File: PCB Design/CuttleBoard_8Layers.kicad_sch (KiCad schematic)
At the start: 170 parts, among them IC1 W25Q256JVEIQ TR, J1 DX07WH24JA3R1200, SW1 SW_Push, SW2 SW_Push, U1 LMR33630CQRNX, U14 STM32H743VIHx, U15 TPS62824ADMQ, U16 ICM-20602, U19 USBLC6-2P6, U20 ACS722xLCTR-10AB, U3 LMR33630CQRNX, U4 ICM-20602, U7 MPRLS0025PA00001A, Y1 NX2016SA

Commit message: Revert "STM32H743 first version"
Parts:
- removed C14, C16: 4.7µF, Capacitor_SMD:C_0402_1005Metric, symbol Device:C
- removed C19: 100nF, Capacitor_SMD:C_0402_1005Metric, symbol Device:C
- removed SW2: SW_Push, Button_Switch_SMD:SW_Push_1P1T-SH_NO_CK_KMR2xxG, symbol Switch:SW_Push
- removed U14: STM32H743VIHx, Package_BGA:TFBGA-100_8x8mm_Layout10x10_P0.8mm, symbol MCU_ST_STM32H7:STM32H743VIHx
- added C21, C22, C23: 4.7µF, Capacitor_SMD:C_0402_1005Metric, symbol Device:C
- added L3: 2.2µH, Inductor_SMD:L_0603_1608Metric, symbol pspice:INDUCTOR
- added U2: STM32H735VGH6, Package_BGA:TFBGA-100_8x8mm_Layout10x10_P0.8mm, symbol ultimateFC-rescue:STM32H735VGH6-lib_ultimateFC
- R20: value 10k -> 2k2; footprint ultimateFC:R_0201_0603Metric_mod -> Resistor_SMD:R_0402_1005Metric; JLCPCB Part # (none) -> C2076947
- R9: value 2k2 -> 10k; footprint Resistor_SMD:R_0402_1005Metric -> ultimateFC:R_0201_0603Metric_mod; JLCPCB Part # C2076947 -> (none)
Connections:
- net CS_FLASH: now also U2.C3 (PE4)
- net CS_IMU1: now also U2.A9 (PD2)
- net EOC_PRESSURE: now also U2.A1 (PE6)
- net GND: now also R20.2, C21.2, C22.2, C23.2, U2.C1 (VSS), U2.D1 (VSSSMPS), U2.D5 (VSS), U2.E7 (VSS), U2.F5 (VSS), U2.H2 (VSSA); no longer R9.2
- net I2C1_SCL: now also U2.D4 (PB6)
- net I2C1_SDA: now also U2.B5 (PB7)
- net I2C2_SCL: now also U2.K7 (PB10)
- net I2C2_SDA: now also U2.J7 (PB11)
- net I2C3_SCL: now also U2.F10 (PA8)
- net I2C3_SDA: now also U2.F9 (PC9)
- net I2C4_SCL: now also U2.A4 (PB8)
- net I2C4_SDA: now also U2.E3 (PB9)
- net INT_IMU1: now also U2.A8 (PD3)
- net NRST: now also R9.2, U2.F2 (NRST); no longer R20.2
- net OSC_IN: now also C7.1, U2.G1 (PH0-OSC_IN); no longer C9.1
- net OSC_OUT: now also C9.1, U2.G2 (PH1-OSC_OUT); no longer C7.1
- net RES_PRESSURE: now also U2.A2 (PE5)
- net SWDCLK: now also U2.C9 (PA14)
- net SWDIO: now also U2.C10 (PA13)
- net UART3_RX: now also U2.H8 (PD9)
- net UART3_TX: now also U2.J9 (PD8)
- net UART7_RX: now also U2.H5 (PE7)
- net UART7_TX: now also U2.J6 (PE8)
- net USB_D+: now also U2.D9 (PA12)
- net USB_D-: now also U2.D10 (PA11)
- net VSense: now also U2.H4 (PC4)
- net curr_sig: now also U2.J3 (PA6)
- net PA9_USB_VBUS_sense: now reaches R14.2, R15.1, TP81.1
- net PA9_USB_VBUS_sense: now also U2.E9 (PA9)
- net +3.3V renamed +3V3
- net +3V3: now also R9.1, U2.C2 (VBAT), U2.D3 (PDR_ON), U2.D6 (VDD), U2.E1 (VDDSMPS), U2.E5 (VDD), U2.E8 (VDD33USB), U2.F6 (VDD), U2.H1 (VDDA), U2.J1 (VREF+); no longer R20.1
- net BOOT0: no longer names the net of SW1.1
- net BOOT0: now also R20.1, U2.A5 (BOOT0); no longer R9.1
- net INT1_IMU3 renamed INT_IMU31
- net INT2_IMU3 renamed INT_IMU32
- net LED_BL renamed PC8_LED_BL
- net PC8_LED_BL: now also U2.G10 (PC8)
- net LED_WT renamed PC7_LED_WT
- net PC7_LED_WT: now also U2.G9 (PC7)
- net SPI3_MISO renamed MISO_GYRO
- net MISO_GYRO: now also U2.B9 (PC11)
- net SPI3_MOSI renamed MOSI_GYRO
- net MOSI_GYRO: now also U2.A10 (PC12)
- net SPI3_SCK renamed SCLK_GYRO
- net SCLK_GYRO: now also U2.B10 (PC10)
- net UART2_RX renamed UART4_RX
- net UART4_RX: now also U2.C7 (PD0)
- net UART2_TX renamed UART4_TX
- net UART4_TX: now also U2.B8 (PD1)
- net UART5_RX renamed UART9_RX
- net UART9_RX: now also U2.G7 (PD14)
- net UART5_TX renamed UART9_TX
- net UART9_TX: now also U2.G8 (PD15)
- new net: C21.1, C22.1, C23.1, L3.2, U2.D8 (VCAP), U2.E2 (VFBSMPS), U2.E6 (VDDLDO), U2.F7 (VDDLDO), U2.G6 (VCAP)
- new net: L3.1, U2.D2 (VLXSMPS)
- new net PC0: U2.F3 (PC0)
- new net PC1: U2.F1 (PC1)
- new net PC2: U2.F4 (PC2_C)
- new net PC3: U2.G4 (PC3_C)
- new net PC6: U2.F8 (PC6)
- new net SPI3_NSS: U2.C8 (PA15)
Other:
- note added: "Application Note (AN5419)"
- note added: "MISO"
- note added: "next to PD10 or PD11"
- moved on the sheet: C10, C11, C12, C13, C17, C18, C24, C28, C29, C3, C30, C31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

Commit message: readded the files after revert, sad
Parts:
- removed C21, C22, C23: 4.7µF, Capacitor_SMD:C_0402_1005Metric, symbol Device:C
- removed L3: 2.2µH, Inductor_SMD:L_0603_1608Metric, symbol pspice:INDUCTOR
- removed U2: STM32H735VGH6, Package_BGA:TFBGA-100_8x8mm_Layout10x10_P0.8mm, symbol ultimateFC-rescue:STM32H735VGH6-lib_ultimateFC
- added C14, C16: 4.7µF, Capacitor_SMD:C_0402_1005Metric, symbol Device:C
- added C19: 100nF, Capacitor_SMD:C_0402_1005Metric, symbol Device:C
- added SW2: SW_Push, Button_Switch_SMD:SW_Push_1P1T-SH_NO_CK_KMR2xxG, symbol Switch:SW_Push
- added U14: STM32H743VIHx, Package_BGA:TFBGA-100_8x8mm_Layout10x10_P0.8mm, symbol MCU_ST_STM32H7:STM32H743VIHx
- R20: value 2k2 -> 10k; footprint Resistor_SMD:R_0402_1005Metric -> ultimateFC:R_0201_0603Metric_mod; JLCPCB Part # C2076947 -> (none)
- R9: value 10k -> 2k2; footprint ultimateFC:R_0201_0603Metric_mod -> Resistor_SMD:R_0402_1005Metric; JLCPCB Part # (none) -> C2076947
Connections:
- net CS_FLASH: now also U14.C3 (PE4)
- net CS_IMU1: now also U14.C7 (PD3)
- net CS_IMU2: now also U14.A7 (PB3)
- net CS_IMU3: now also U14.A6 (PB4)
- net EOC_PRESSURE: now also U14.A2 (PC13)
- net GND: now also R9.2, C14.2, C16.2, C19.2, SW2.1, U14.C2 (VSS), U14.E4 (VSS), U14.E5 (VSS), U14.E6 (VSS), U14.G1 (VSSA), U14.J1 (VSS); no longer R20.2
- net I2C1_SCL: now also U14.B4 (PB8)
- net I2C1_SDA: now also U14.A4 (PB9)
- net I2C2_SCL: now also U14.J7 (PB10)
- net I2C2_SDA: now also U14.K7 (PB11)
- net I2C3_SCL: now also U14.D9 (PA8)
- net I2C3_SDA: now also U14.E9 (PC9)
- net I2C4_SCL: now also U14.B5 (PB6)
- net I2C4_SDA: now also U14.A5 (PB7)
- net INT_IMU1: now also U14.B7 (PD2)
- net INT_IMU2: now also U14.A8 (PA15)
- net NRST: now also R20.2, C19.1, SW2.2, U14.E1 (NRST); no longer R9.2
- net OSC_IN: now also C9.1, U14.C1 (PH0); no longer C7.1
- net OSC_OUT: now also C7.1, U14.D1 (PH1); no longer C9.1
- net RES_PRESSURE: now also U14.B3 (PE3)
- net SWDCLK: now also U14.A9 (PA14)
- net SWDIO: now also U14.A10 (PA13)
- net UART3_RX: now also U14.J9 (PD9)
- net UART3_TX: now also U14.K9 (PD8)
- net UART7_RX: now also U14.H5 (PE7)
- net USB_D+: now also U14.B10 (PA12)
- net USB_D-: now also U14.C10 (PA11)
- net VSense: now also U14.G4 (PC4)
- net curr_sig: now also U14.J3 (PA6)
- net +3.3V: now reaches R20.1
- net +3.3V: now also C20.1, C31.1, C32.1, C33.1, C34.1, C35.1, C36.1, C37.1, C38.1, C39.1, C40.1, C41.1, C42.1, C43.1, C44.1, C45.1, C46.1, C47.1, C49.1, FB7.1, IC1.8 (VCC), JP1.1 (A), R18.1, R19.1, R2.1, R21.1, R22.1, R23.1, R3.1, R7.1, R8.1, SW1.2, TP44.1, TP45.1, TP7.1, TP8.1, TP9.1, U16.1 (VDDIO), U16.16 (VDD), U17.5 (VDD_IO), U17.8 (VDD), U20.8 (VCC), U4.1 (VDDIO), U4.16 (VDD), U7.12 (VDD), U14.B2 (VBAT), U14.D2 (VDD), U14.F4 (VDDLDO), U14.F5 (VDD), U14.F6 (VDD33_USB), U14.F7 (PDR_ON), U14.H1 (VDDA), U14.K1 (VDD); no longer SW1.1
- removed net +3V3: C20.1, C31.1, C32.1, C33.1, C34.1, C35.1, C36.1, C37.1, C38.1, C39.1, C40.1, C41.1, C42.1, C43.1, C44.1, C45.1, C46.1, C47.1, C49.1, FB7.1, IC1.8 (VCC), JP1.1 (A), R18.1, R19.1, R2.1, R21.1, R22.1, R23.1, R3.1, R7.1, R8.1, R9.1, SW1.2, TP44.1, TP45.1, TP7.1, TP8.1, TP9.1, U16.1 (VDDIO), U16.16 (VDD), U17.5 (VDD_IO), U17.8 (VDD), U20.8 (VCC), U4.1 (VDDIO), U4.16 (VDD), U7.12 (VDD)
- net INT_IMU31 renamed INT1_IMU3
- net INT1_IMU3: now also U14.C4 (PE1)
- net INT_IMU32 renamed INT2_IMU3
- net INT2_IMU3: now also U14.C5 (PB5)
- net MISO_GYRO renamed SPI3_MISO
- net SPI3_MISO: now also U14.B8 (PC11)
- net MOSI_GYRO renamed SPI3_MOSI
- net SPI3_MOSI: now also U14.C8 (PC12)
- net PA9_USB_VBUS_sense: no longer names the net of R14.2, R15.1, TP81.1
- net PC7_LED_WT renamed LED_WT
- net LED_WT: now also U14.F9 (PC8)
- net PC8_LED_BL renamed LED_BL
- net LED_BL: now also U14.H9 (PD10)
- net SCLK_GYRO renamed SPI3_SCK
- net SPI3_SCK: now also U14.B9 (PC10)
- net UART4_RX renamed UART2_RX
- net UART2_RX: now also U14.C6 (PD6)
- net UART4_TX renamed UART2_TX
- net UART2_TX: now also U14.B6 (PD5)
- net UART9_RX renamed UART5_RX
- net UART5_RX: now also U14.K8 (PB12)
- net UART9_TX renamed UART5_TX
- net UART5_TX: now also U14.J8 (PB13)
- new net: C14.1, U14.E7 (VCAP)
- new net: C16.1, U14.F8 (VCAP)
- new net BOOT0: R9.1, SW1.1, U14.D5 (BOOT0)
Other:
- note removed: "Application Note (AN5419)"
- note removed: "MISO"
- note removed: "next to PD10 or PD11"
- moved on the sheet: C10, C11, C12, C13, C17, C18, C24, C28, C29, C3, C30, C31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

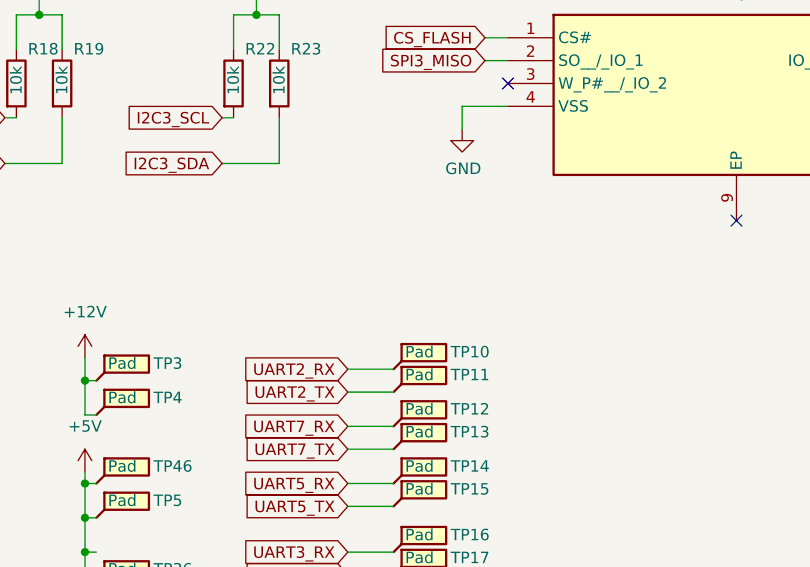
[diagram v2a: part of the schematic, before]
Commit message: Fixed castellated edge and some vias
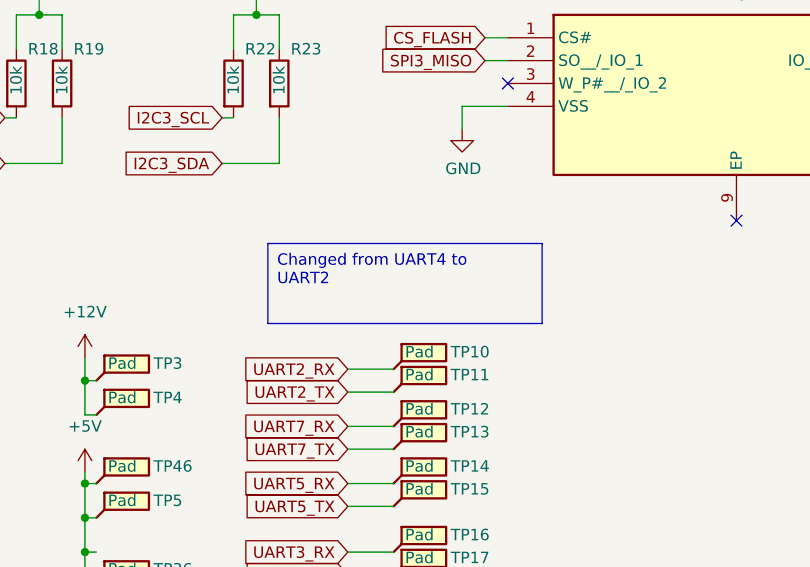
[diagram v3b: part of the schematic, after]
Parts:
- R20: footprint ultimateFC:R_0201_0603Metric_mod -> Resistor_SMD:R_0402_1005Metric
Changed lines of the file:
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@@
 		)
 	)
+	(text_box "Changed from UART4 to UART2"
+		(exclude_from_sim no)
+		(at 163.83 49.53 0)
+		(size 30.48 8.89)
+		(stroke
+			(width 0)
+			(type default)
+		)
+		(fill
+			(type none)
+		)
+		(effects
+			(font
+				(size 1.27 1.27)
+			)
+			(justify left top)
+		)
+	)
 	(text "assign IMU INT line"
 		(exclude_from_sim no)
@@
 			)
 		)
-		(property "Footprint" "ultimateFC:R_0201_0603Metric_mod"
+		(property "Footprint" "Resistor_SMD:R_0402_1005Metric"
 			(at 295.402 129.54 90)
 			(effects

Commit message: fixed errors/warnings, looks OK, needs doublechecking
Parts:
- D10, D6, D8, D9: footprint SBRT10U50SP513 -> SBRT10U50SP5:SBRT10U50SP513
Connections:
- net UART7_TX: now also U14.J5 (PE8)
- no-connect marks 69 -> 68
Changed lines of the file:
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@@
 	)
 	(no_connect
-		(at 359.41 81.28)
-	)
-	(no_connect
 		(at 405.13 53.34)
 	)
@@
 	(wire
 		(pts
+			(xy 349.25 81.28) (xy 359.41 81.28)
+		)
+		(stroke
+			(width 0)
+			(type default)
+		)
+	)
+	(wire
+		(pts
 			(xy 368.3 373.38) (xy 341.63 373.38)
 		)
@@
 		)
 	)
+	(global_label "UART7_TX"
+		(shape input)
+		(at 349.25 81.28 180)
+		(effects
+			(font
+				(size 1.27 1.27)
+			)
+			(justify right)
+		)
+		(property "Intersheetrefs" "${INTERSHEET_REFS}"
+			(at 349.25 81.28 0)
+			(effects
+				(font
+					(size 1.27 1.27)
+				)
+				(hide yes)
+			)
+		)
+	)
 	(global_label "I2C3_SDA"
 		(shape input)
@@
 			)
 		)
-		(property "Footprint" "SBRT10U50SP513"
+		(property "Footprint" "SBRT10U50SP5:SBRT10U50SP513"
 			(at 57.15 119.71 0)
 			(effects
@@
 			)
 		)
-		(property "Footprint" "SBRT10U50SP513"
+		(property "Footprint" "SBRT10U50SP5:SBRT10U50SP513"
 			(at 130.48 224.79 0)
 			(effects
@@
 			)
 		)
-		(property "Footprint" "SBRT10U50SP513"
+		(property "Footprint" "SBRT10U50SP5:SBRT10U50SP513"
 			(at 57.15 165.43 0)
 			(effects
@@
 			)
 		)
-		(property "Footprint" "SBRT10U50SP513"
+		(property "Footprint" "SBRT10U50SP5:SBRT10U50SP513"
 			(at 192.71 224.79 0)
 			(effects

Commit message: finished BOM for JLCPCB, switched 0201 for 0402, cleaned up silkscreen
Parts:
- C1, C30: JLCPCB Part # (none) -> C18164608
- C20, C24, C49: footprint ultimateFC:C_0201_0603Metric_mod -> Capacitor_SMD:C_0402_1005Metric; JLCPCB Part # (none) -> C106256
- C26, C28, C29: JLCPCB Part # (none) -> C95839
- C27: footprint ultimateFC:C_0201_0603Metric_mod -> Capacitor_SMD:C_0402_1005Metric; JLCPCB Part # (none) -> C2443241
- D10, D6, D8, D9: JLCPCB Part # (none) -> C2978909
- FB1, FB2, FB3, FB5, FB6, FB7: JLCPCB Part # (none) -> C113030
- H1, H2, H3, H4, JP1, TP1, TP10, TP11, TP12, TP13, TP14, TP15, TP16, TP17, TP18, TP19, TP2, TP20, TP21, TP22, TP23, TP24, TP25, TP26, TP27, TP28, TP29, TP3, TP30, TP31, TP32, TP33, TP35, TP36, TP37, TP38, TP39, TP4, TP40, TP41, TP42, TP43, TP44, TP45, TP46, TP47, TP48, TP5, TP6, TP7, TP8, TP81, TP88, TP9, U17: now not fitted
- J1: JLCPCB Part # (none) -> C3197973
- R11: JLCPCB Part # (none) -> C2998048
- R16: footprint ultimateFC:R_0201_0603Metric_mod -> Capacitor_SMD:C_0402_1005Metric; JLCPCB Part # (none) -> C170322
- R17: footprint ultimateFC:R_0201_0603Metric_mod -> Resistor_SMD:R_0402_1005Metric; JLCPCB Part # (none) -> C431822
- R18, R19, R2, R20, R21, R22, R23, R29, R3, R8: JLCPCB Part # (none) -> C60490
- R26, R27: footprint ultimateFC:R_0201_0603Metric_mod -> Capacitor_SMD:C_0402_1005Metric; JLCPCB Part # (none) -> C105873
- R30: footprint ultimateFC:R_0201_0603Metric_mod -> Resistor_SMD:R_0402_1005Metric; JLCPCB Part # (none) -> C844716
- U14: JLCPCB Part # (none) -> C964146
- U15: JLCPCB Part # (none) -> C2862909
- U16, U4: JLCPCB Part # (none) -> C97633
- U19: JLCPCB Part # (none) -> C22390016
- U20: JLCPCB Part # (none) -> C459316
- Y1: JLCPCB Part # (none) -> C843258

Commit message: final push
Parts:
- H1, H2, H3, H4, JP1, TP1, TP10, TP11, TP12, TP13, TP14, TP15, TP16, TP17, TP18, TP19, TP2, TP20, TP21, TP22, TP23, TP24, TP25, TP26, TP27, TP28, TP29, TP3, TP30, TP31, TP32, TP33, TP35, TP36, TP37, TP38, TP39, TP4, TP40, TP41, TP42, TP43, TP44, TP45, TP46, TP47, TP48, TP5, TP6, TP7, TP8, TP81, TP88, TP9, U17: now fitted
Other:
- note added: "Nucleo doesn't have it is it necessary (?)"
- note added: "TVS diode for protection between NRST and GND"
- note added: "seems unnecessary"
- moved on the sheet: C19, R20, R9, SW1, SW2
